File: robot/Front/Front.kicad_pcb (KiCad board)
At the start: 2 copper layers, 0 parts

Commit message: Cleanup, start PDB Front
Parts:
- added C1: 100n, Capacitors_SMD:C_1206_HandSoldering, F.Cu at (172.5, 53.5)
- added C19: 1µ, Capacitors_SMD:C_1206_HandSoldering, F.Cu at (124.3, 78.4)
- added C2: 10µ, Capacitors_SMD:C_1206_HandSoldering, F.Cu at (124.3, 81.5)
- added C3: 100n, Capacitors_SMD:C_1206_HandSoldering, F.Cu at (218.6, 158.1)
- added C6: 10µ, Capacitors_SMD:C_1206_HandSoldering, F.Cu at (116.8, 81.6)
- added D1: BLUE, LED_SMD:LED_0805_2012Metric_Pad1.15x1.40mm_HandSolder, F.Cu at (212.1, 177.8)
- added D2: GREEN, LED_SMD:LED_0805_2012Metric_Pad1.15x1.40mm_HandSolder, F.Cu at (207.0, 178.8)
- added H1: VBUS, Custom:Mounting_Pad_Power, F.Cu at (197.5, 102.5)
- added H10: M1B2, Custom:Mounting_Pad_Signal, F.Cu at (223.1, 144.1)
- added H11: BAT_MON, Custom:Mounting_Pad_Signal, F.Cu at (214.2, 168.2)
- added H12: ED1, Custom:Mounting_Pad_Signal, F.Cu at (221.3, 162.2)
- added H13: ED2, Custom:Mounting_Pad_Signal, F.Cu at (218.2, 168.2)
- added H14: OSDA, Custom:Mounting_Pad_Signal, F.Cu at (210.7, 173.8)
- added H15: OSCL, Custom:Mounting_Pad_Signal, F.Cu at (227.4, 161.4)
- added H16: ORST, Custom:Mounting_Pad_Signal, F.Cu at (214.7, 173.2)
- added H17: VBAT_SWITCH, Custom:Mounting_Pad_Power, F.Cu at (233.2, 102.5)
- added H18: GND, Custom:Mounting_Pad_Power, F.Cu at (194.2, 143.5)
- added H19: GND, Custom:Mounting_Pad_Power, F.Cu at (194.2, 102.5)
- added H2: M_~SLP, Custom:Mounting_Pad_Signal, F.Cu at (225.7, 144.1)
- added H20: 3V3, Custom:Mounting_Pad_Power, F.Cu at (197.8, 143.5)
- added H21: GND, Custom:Mounting_Pad_Power, F.Cu at (236.8, 102.5)
- added H22: GND, Custom:Mounting_Pad_Power, F.Cu at (236.8, 143.5)
- added H23: 3V3, Custom:Mounting_Pad_Power, F.Cu at (233.2, 143.5)
- added H3: M2B2, Custom:Mounting_Pad_Signal, F.Cu at (205.3, 144.1)
- added H4: M2B1, Custom:Mounting_Pad_Signal, F.Cu at (207.9, 144.1)
- added H5: M2A2, Custom:Mounting_Pad_Signal, F.Cu at (210.4, 144.1)
- added H6: M2A1, Custom:Mounting_Pad_Signal, F.Cu at (212.9, 144.1)
- added H7: M1A1, Custom:Mounting_Pad_Signal, F.Cu at (215.5, 144.1)
- added H8: M1A2, Custom:Mounting_Pad_Signal, F.Cu at (218.0, 144.1)
- added H9: M1B1, Custom:Mounting_Pad_Signal, F.Cu at (220.6, 144.1)
- added J1: USB_B_Micro, Connectors_USB:USB_Micro-B_Molex_47346-0001, F.Cu at (173.9, 48.7)
- added Q1: BC849, Package_TO_SOT_SMD:SOT-23, F.Cu at (230.6, 163.0)
- added Q2: BC849, Package_TO_SOT_SMD:SOT-23, F.Cu at (217.9, 173.0)
- added R1: 10k, Resistors_SMD:R_1206_HandSoldering, F.Cu at (139.4, 80.1)
- added R18: 10k, Resistors_SMD:R_1206_HandSoldering, F.Cu at (116.8, 78.4)
- added R2: 10k, Resistors_SMD:R_1206_HandSoldering, F.Cu at (200.8, 177.9)
- added R3: 150, Resistors_SMD:R_1206_HandSoldering, F.Cu at (131.9, 81.7)
- added R4: 150, Resistors_SMD:R_1206_HandSoldering, F.Cu at (131.9, 78.4)
- added SW2: SW_Push, Buttons_Switches_THT:SW_PUSH_SMALL, F.Cu at (209.8, 160.9)
- added U1: CH340C, Package_SO:SOIC-16_3.9x9.9mm_P1.27mm, F.Cu at (200.6, 162.3)
- added U10: ESP32-WROOM-32, RF_Module:ESP32-WROOM-32, F.Cu at (215.5, 130.5)
- added U2: CJVL53L0XV2, Custom:CJVL53L0XV2, F.Cu at (123.5, 99.2)
- added U3: LD1117S33CTR, Package_TO_SOT_SMD:SOT-223, F.Cu at (201.3, 172.1)
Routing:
- added copper zone on F.Cu, net +3V3
- added copper zone on B.Cu, net GND
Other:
- board outline added: 46 x 46 mm

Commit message: Front PCB
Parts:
- removed C19: 1µ, Capacitors_SMD:C_1206_HandSoldering
- C1, C2, C3, C6: footprint Capacitors_SMD:C_1206_HandSoldering -> Capacitors_SMD:C_1206
- R1, R18, R2, R3, R4: footprint Resistors_SMD:R_1206_HandSoldering -> Resistors_SMD:R_1206
- SW2: footprint Buttons_Switches_THT:SW_PUSH_SMALL -> Button_Switch_SMD:Panasonic_EVQPUJ_EVQPUA
- U2: footprint Custom:CJVL53L0XV2 -> Custom:CJVL53L0XV2_NoMountHoles
- moved R18 119.6 mm to (231.8, 111.5), turned to 90 degrees
- moved C2 114.7 mm to (232.8, 119.0), turned to 90 degrees
- moved R1 107.4 mm to (231.8, 135.0)
- moved R3 93.8 mm to (222.5, 105.8)
- moved C6 88.0 mm to (197.0, 117.8), turned to 180 degrees
- moved C1 87.5 mm to (228.5, 120.8), turned to 180 degrees
- moved R4 81.3 mm to (208.5, 105.8), turned to 180 degrees
- moved U2 79.3 mm to (194.2, 135.0), turned to 270 degrees
- moved D2 76.9 mm to (209.0, 102.0)
- moved D1 76.5 mm to (222.0, 102.0), turned to 180 degrees
- moved H14 73.2 mm to (224.5, 102.0), turned to 180 degrees
- moved H16 72.8 mm to (229.5, 102.0), turned to 180 degrees
- moved J1 67.8 mm to (215.5, 102.2), turned to 180 degrees
- moved H11 67.5 mm to (201.5, 102.0), turned to 180 degrees
- moved U3 61.0 mm to (197.0, 111.2), turned to 90 degrees
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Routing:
- net Net-(Q1-Pad2): track 0.00 -> 19.2 mm
- net Net-(Q2-Pad2): track 0.00 -> 12.6 mm
- net /M2_BOUT2: track 0.00 -> 10.6 mm
- net /M1_M2_~SLEEP: track 0.00 -> 9.66 mm
- net /M2_BOUT1: track 0.00 -> 9.26 mm
- net /~RST: track 0.00 -> 8.89 mm
- net /M1_BOUT2: track 0.00 -> 8.12 mm
- net Net-(C1-Pad1): track 0.00 -> 8.10 mm
- net /M2_AOUT2: track 0.00 -> 8.01 mm
- net /M2_AOUT1: track 0.00 -> 6.84 mm
- net /M1_BOUT1: track 0.00 -> 6.83 mm
- net /M1_AOUT1: track 0.00 -> 6.31 mm
- net /M1_AOUT2: track 0.00 -> 6.30 mm
- net VBUS: track 0.00 -> 6.18 mm
- net Net-(D1-Pad2): track 0.00 -> 3.78 mm
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- added copper zone on B.Cu, net +3V3
- added copper zone on F.Cu, net GND
- removed copper zone on F.Cu, net +3V3
- removed copper zone on B.Cu, net GND

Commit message: Front Routing
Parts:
- added H24: 3V3, Custom:Mounting_Pad_Power, F.Cu at (197.8, 102.5)
- moved H1 3.50 mm to (201.2, 102.5)
- moved H11 3.50 mm to (205.0, 102.0)
- moved C2 0.25 mm to (233.0, 119.0)
- moved C3 0.25 mm to (235.5, 119.0)
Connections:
- net Net-(J1-Pad2) renamed /D-
- net Net-(J1-Pad3) renamed /D+
- C2 pad 1: VBUS -> +3V3
- C3 pad 1: VBUS -> +3V3
- U1 pad 16: VBUS -> +3V3
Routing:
- net +3V3: track 0.00 -> 134.8 mm, vias 0 -> 6
- net /~RST: track 8.89 -> 75.1 mm
- net VBUS: track 6.18 -> 52.8 mm, vias 0 -> 3
- net /STATUS_LED_GRN: track 0.00 -> 44.6 mm
- net /D-: track 0.00 -> 40.5 mm
- net /D+: track 0.00 -> 38.6 mm
- net /OLED_SDA: track 0.00 -> 36.6 mm, vias 0 -> 2
- net /BAT_MON: track 0.00 -> 36.4 mm, vias 0 -> 2
- net /ED_IN2: track 0.00 -> 30.5 mm
- net /OLED_SCL: track 0.00 -> 30.4 mm, vias 0 -> 2
- net /ED_IN1: track 0.00 -> 24.0 mm, vias 0 -> 2
- net /OD_SDA: track 0.00 -> 16.2 mm
- net /OD_SHUT: track 0.00 -> 16.2 mm, vias 0 -> 2
- net /OD_SCL: track 0.00 -> 15.7 mm
- net /OD_INTERRUPT: track 0.00 -> 14.6 mm
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- added copper zone on B.Cu, net GND
- removed copper zone on B.Cu, net +3V3
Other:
- net class Power added: clearance 0.3, trace_width 0.5, via_dia 1, via_drill 0.5

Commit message: Finish Front
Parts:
- H17: value VBAT_SWITCH -> VBAT_SW
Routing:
- net /STATUS_LED_BLUE: track 0.00 -> 39.2 mm, vias 0 -> 2
- net /OLED_~RES: track 2.55 -> 25.4 mm, vias 0 -> 2
- net +3V3: track 134.8 -> 140.7 mm, vias 6 -> 7
- net GND: vias 11 -> 43
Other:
- outline, holes or cut-outs redrawn

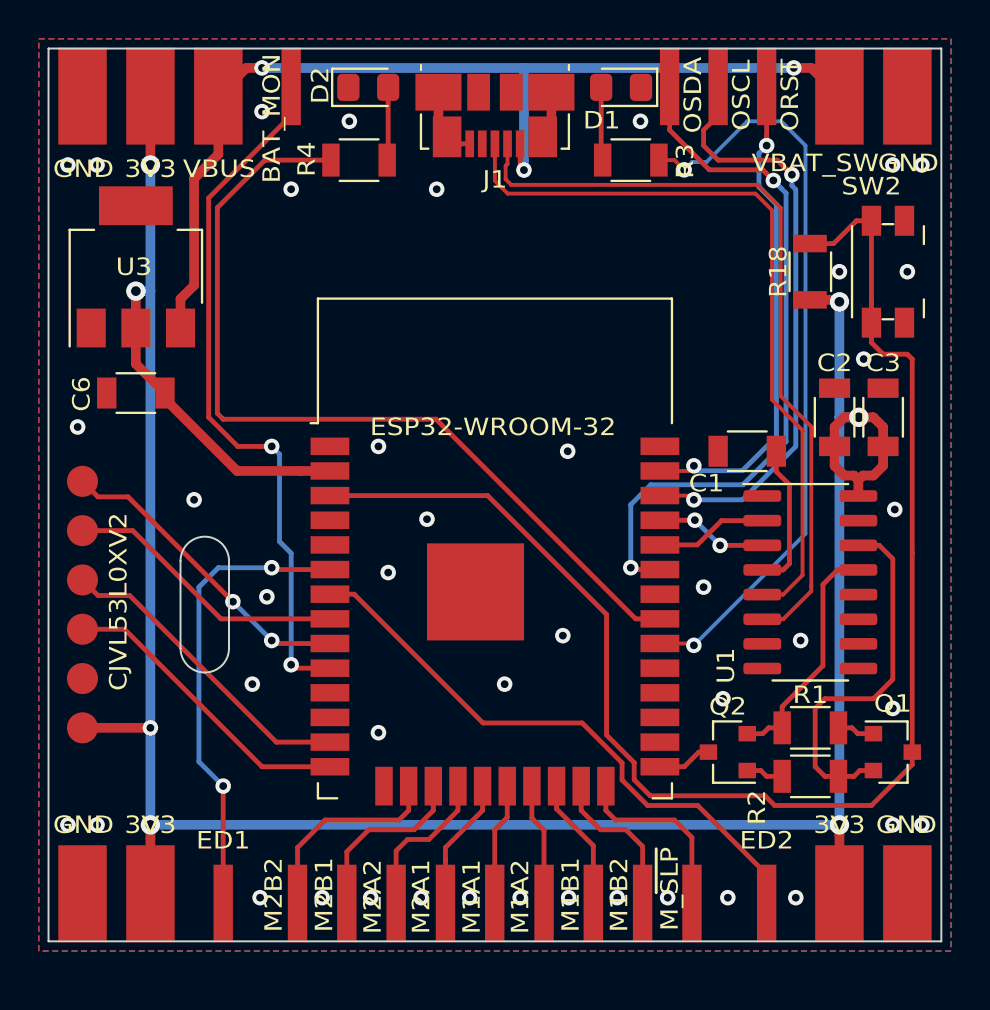
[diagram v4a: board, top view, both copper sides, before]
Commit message: Swap 3V3 and VBUS, Fix Cutout, small changes
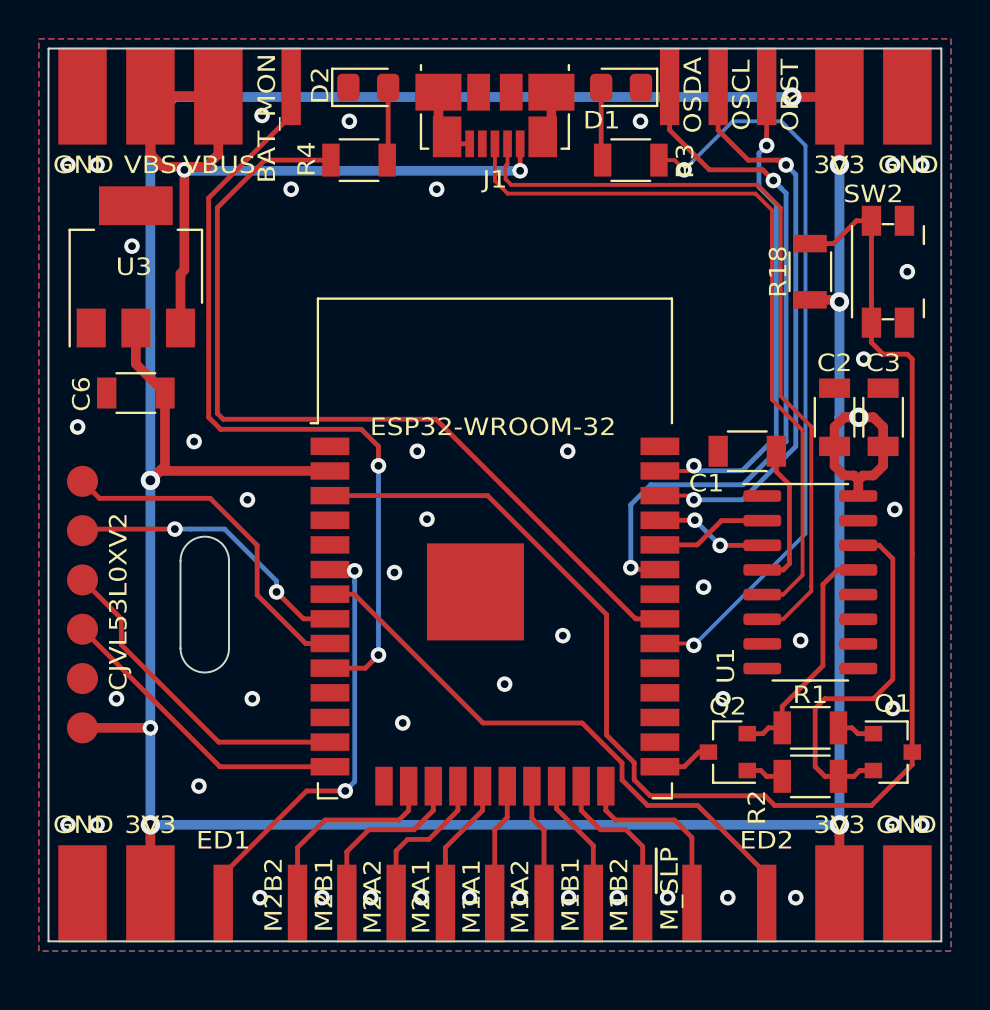
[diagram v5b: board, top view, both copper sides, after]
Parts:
- H17: value VBAT_SW -> VBS
- moved H17 35.5 mm to (197.8, 102.5)
- moved H24 35.5 mm to (233.2, 102.5)
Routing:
- net +3V3: track 140.7 -> 187.6 mm, vias 7 -> 8
- net VBUS: track 52.8 -> 40.6 mm, vias 3 -> 2
- net /BAT_MON: track 36.4 -> 41.7 mm
- net /ED_IN1: track 24.0 -> 22.5 mm
- net /OD_SHUT: track 16.2 -> 17.7 mm, vias 2 -> 0
- net /OD_SDA: track 16.2 -> 17.0 mm
- net /OD_INTERRUPT: track 14.6 -> 15.0 mm, vias 0 -> 2
- net GND: vias 43 -> 45

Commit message: Renumber and more Bottom
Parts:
- H10: value M1B2 -> M2B2
- H3: value M2B2 -> M1B2
- H4: value M2B1 -> M1B1
- H5: value M2A2 -> M1A2
- H6: value M2A1 -> M1A1
- H7: value M1A1 -> M2A1
- H8: value M1A2 -> M2A2
- H9: value M1B1 -> M2B1
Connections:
- H10 pad 1: /M1_BOUT2 -> /M2_BOUT2
- H3 pad 1: /M2_BOUT2 -> /M1_BOUT2
- H4 pad 1: /M2_BOUT1 -> /M1_BOUT1
- H5 pad 1: /M2_AOUT2 -> /M1_AOUT2
- H6 pad 1: /M2_AOUT1 -> /M1_AOUT1
- H7 pad 1: /M1_AOUT1 -> /M2_AOUT1
- H8 pad 1: /M1_AOUT2 -> /M2_AOUT2
- H9 pad 1: /M1_BOUT1 -> /M2_BOUT1
- U10 pad 16: /M2_BOUT2 -> /M1_BOUT2
- U10 pad 17: /M2_BOUT1 -> /M1_BOUT1
- U10 pad 18: /M2_AOUT2 -> /M1_AOUT2
- U10 pad 19: /M2_AOUT1 -> /M1_AOUT1
- U10 pad 20: /M1_AOUT1 -> /M2_AOUT1
- U10 pad 21: /M1_AOUT2 -> /M2_AOUT2
- U10 pad 22: /M1_BOUT1 -> /M2_BOUT1
- U10 pad 23: /M1_BOUT2 -> /M2_BOUT2
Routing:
- net /M2_BOUT2: track 10.6 -> 8.12 mm
- net /M1_BOUT2: track 8.12 -> 10.6 mm
- net /M2_BOUT1: track 9.26 -> 6.83 mm
- net /M1_BOUT1: track 6.83 -> 9.26 mm
- net /M2_AOUT2: track 8.01 -> 6.30 mm
- net /M1_AOUT2: track 6.30 -> 8.01 mm
- net /M2_AOUT1: track 6.84 -> 6.31 mm
- net /M1_AOUT1: track 6.31 -> 6.84 mm
- net Net-(Q2-Pad2): vias 0 -> 1
- net GND: vias 45 -> 44

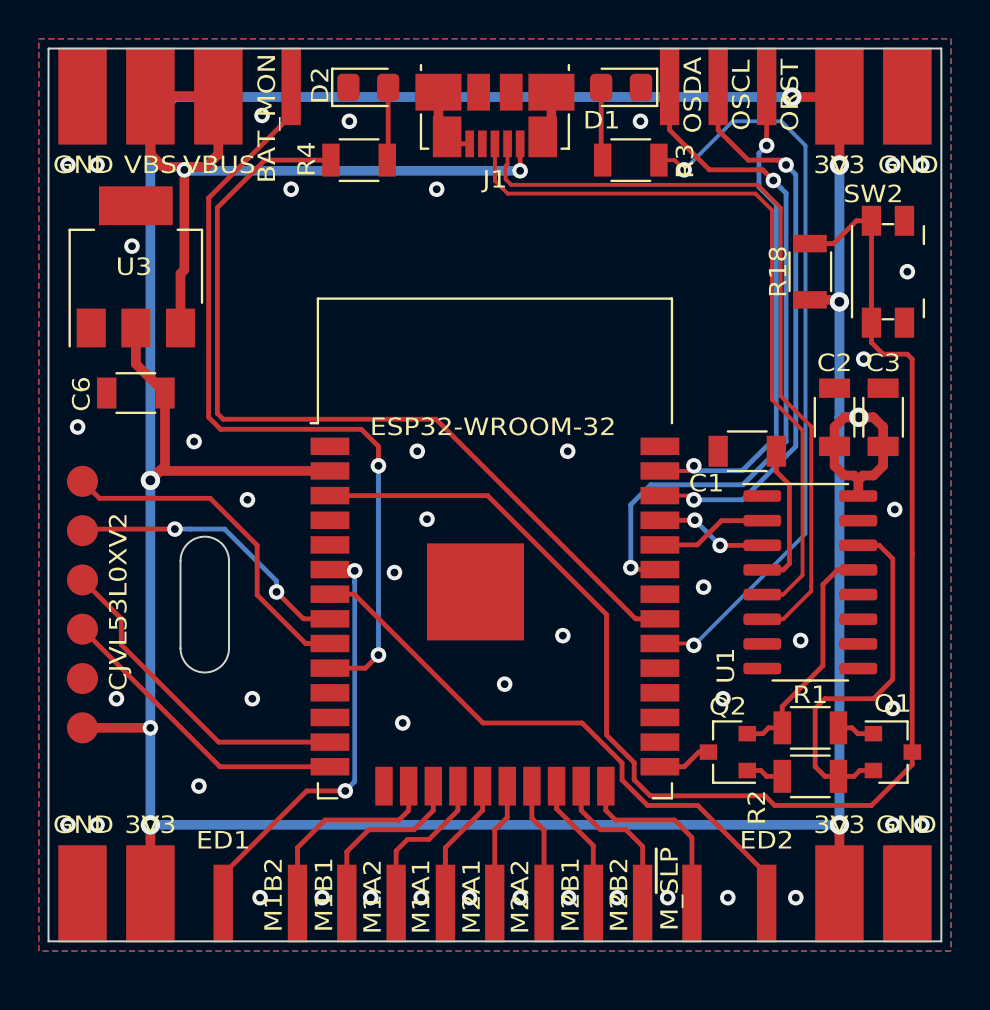
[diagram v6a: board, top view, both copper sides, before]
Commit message: Shrink design
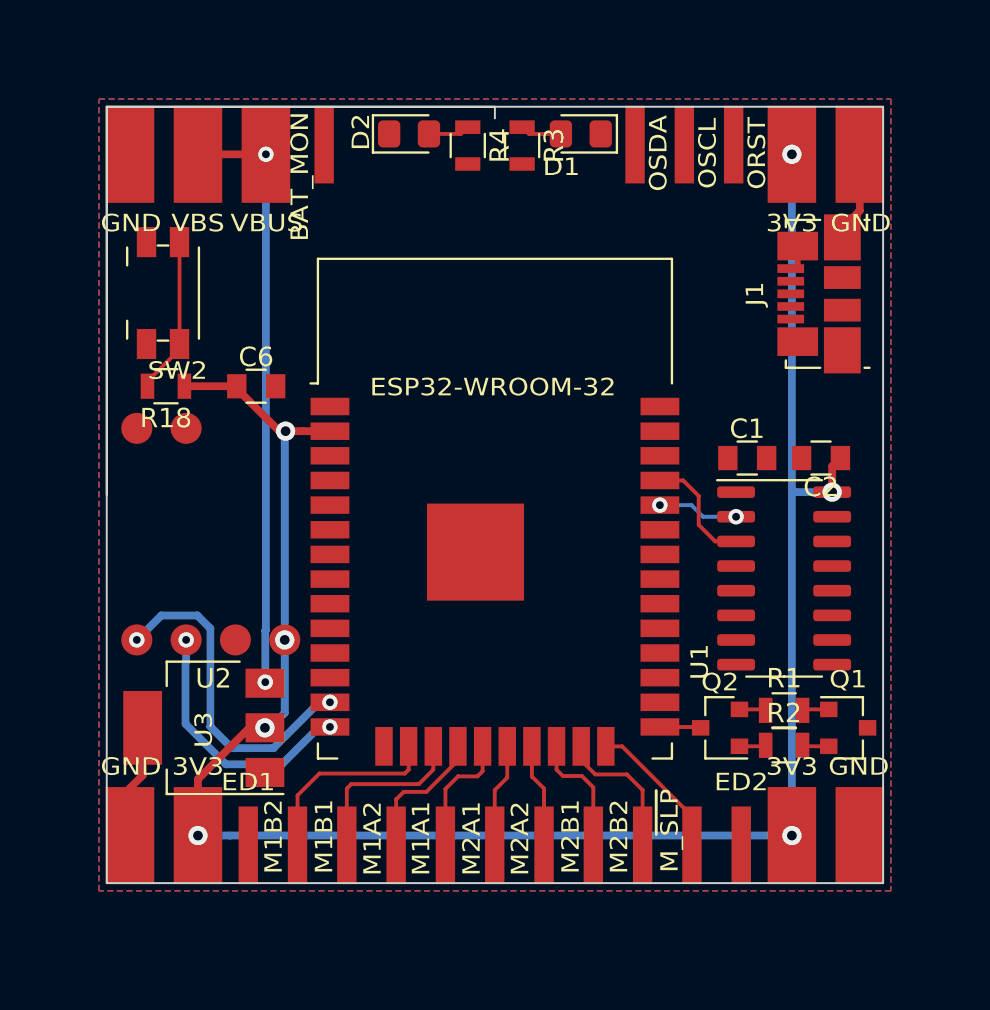
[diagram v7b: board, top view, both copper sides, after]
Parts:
- removed C3: 100n, Capacitors_SMD:C_1206
- C1, C2, C6: footprint Capacitors_SMD:C_1206 -> Capacitors_SMD:C_0805
- R1, R18, R2, R3, R4: footprint Resistors_SMD:R_1206 -> Resistors_SMD:R_0805
- U2: footprint Custom:CJVL53L0XV2_NoMountHoles -> Custom:GYVL53L0X_NoMountingHoles
- moved SW2 37.4 mm to (198.4, 112.6), turned to 90 degrees
- moved R18 33.7 mm to (198.6, 117.4), turned to 180 degrees
- moved U3 24.0 mm to (200.5, 135.0), turned to 180 degrees
- moved J1 20.7 mm to (233.4, 112.6), turned to 90 degrees
- moved U2 11.6 mm to (204.7, 129.9), turned to 0 degrees
- moved C6 6.21 mm to (203.2, 117.4), turned to 0 degrees
- moved R3 5.65 mm to (216.9, 105.0), turned to 270 degrees
- moved R4 5.65 mm to (214.1, 105.0), turned to 270 degrees
- moved H1 3.87 mm to (203.7, 105.5)
- moved H17 3.87 mm to (200.2, 105.5)
- moved H18 3.87 mm to (196.7, 140.6)
- moved H19 3.87 mm to (196.7, 105.5)
- moved H20 3.87 mm to (200.2, 140.6)
- moved H21 3.87 mm to (234.3, 105.5)
- moved H22 3.87 mm to (234.3, 140.6)
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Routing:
- net +3V3: track 187.6 -> 101.6 mm, vias 8 -> 7
- net /~RST: track 74.9 -> 8.11 mm
- net /STATUS_LED_GRN: track 44.6 -> 0.00 mm
- net /BAT_MON: track 41.7 -> 0.00 mm, vias 2 -> 0
- net /D-: track 40.2 -> 0.00 mm
- net /STATUS_LED_BLUE: track 39.2 -> 0.00 mm, vias 2 -> 0
- net /D+: track 38.8 -> 0.00 mm
- net /OLED_SDA: track 36.5 -> 0.00 mm, vias 2 -> 0
- net /OLED_SCL: track 30.9 -> 0.00 mm, vias 2 -> 0
- net /ED_IN2: track 30.5 -> 0.00 mm
- net /OLED_~RES: track 25.4 -> 0.00 mm, vias 2 -> 0
- net /ED_IN1: track 22.5 -> 0.00 mm, vias 2 -> 0
- net Net-(Q1-Pad2): track 19.2 -> 1.37 mm
- net /OD_SHUT: track 17.7 -> 0.00 mm
- net /OD_INTERRUPT: track 15.0 -> 0.00 mm, vias 2 -> 0
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- added copper zone on B.Cu, net (none)
- removed copper zone on B.Cu, net GND
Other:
- board size 46 x 46 mm -> 40 x 40 mm
- net class Default: trace_width 0.25 -> 0.2
- net class Power: trace_width 0.5 -> 0.4

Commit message: Finish Front redesign
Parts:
- removed C6: 10µ, Capacitors_SMD:C_0805
- C2: value 10µ -> 22µ
- H11: value BAT_MON -> BTMN
- U3: value LD1117S33CTR -> SPX3819M5-L-3-3; footprint Package_TO_SOT_SMD:SOT-223 -> Package_TO_SOT_SMD:SOT-23-5
- moved J1 35.9 mm to (197.5, 112.6), turned to 270 degrees
- moved SW2 34.1 mm to (232.5, 112.6), turned to 270 degrees
- moved R18 34.0 mm to (232.6, 117.4)
- moved C1 30.8 mm to (197.7, 119.8), turned to 90 degrees
- moved R1 29.7 mm to (200.7, 134.0)
- moved R2 29.7 mm to (200.7, 136.0)
- moved U1 29.7 mm to (200.7, 127.4)
- moved Q1 29.7 mm to (204.0, 135.0)
- moved Q2 29.7 mm to (197.4, 135.0)
- moved U2 29.6 mm to (234.2, 129.9)
- moved C2 28.6 mm to (203.7, 119.8), turned to 90 degrees
- moved U3 15.2 mm to (200.7, 119.8), turned to 270 degrees
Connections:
- U10 pad 10: /BAT_MON -> (no net)
- U10 pad 12: (no net) -> /ED_IN1
- U10 pad 13: /OD_SDA -> (no net)
- U10 pad 14: /OD_SCL -> (no net)
- U10 pad 27: (no net) -> /ED_IN2
- U10 pad 28: (no net) -> /OD_SCL
- U10 pad 29: (no net) -> /OD_SDA
- U10 pad 30: /STATUS_LED_BLUE -> /OD_SHUT
- U10 pad 31: /STATUS_LED_GRN -> /OD_INTERRUPT
- U10 pad 6: /ED_IN1 -> /BAT_MON
- U10 pad 7: /ED_IN2 -> /STATUS_LED_GRN
- U10 pad 8: /OD_INTERRUPT -> /STATUS_LED_BLUE
- U10 pad 9: /OD_SHUT -> (no net)
- U3 pad 1: GND -> VBUS
- U3 pad 2: +3V3 -> GND
- U3 pad 4: GND -> (no net)
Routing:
- net /~RST: track 8.11 -> 49.8 mm, vias 0 -> 2
- net /STATUS_LED_BLUE: track 0.00 -> 36.0 mm
- net /STATUS_LED_GRN: track 0.00 -> 32.4 mm
- net /GPIO0: track 2.12 -> 31.0 mm, vias 0 -> 2
- net /OLED_SDA: track 0.00 -> 26.2 mm
- net /BAT_MON: track 0.00 -> 23.8 mm, vias 0 -> 2
- net /D-: track 0.00 -> 23.2 mm, vias 0 -> 2
- net /TXD-RXD: track 4.17 -> 26.6 mm
- net /RXD-TXD: track 6.10 -> 27.9 mm, vias 0 -> 2
- net /D+: track 0.00 -> 20.5 mm, vias 0 -> 2
- net /OLED_SCL: track 0.00 -> 20.3 mm
- net /OD_INTERRUPT: track 0.00 -> 17.7 mm
- net /OLED_~RES: track 0.00 -> 16.7 mm, vias 0 -> 2
- net /OD_SHUT: track 0.00 -> 15.2 mm
- net /ED_IN1: track 0.00 -> 15.2 mm
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- added copper zone on B.Cu, net GND
- removed copper zone on B.Cu, net (none)
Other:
- outline, holes or cut-outs redrawn
